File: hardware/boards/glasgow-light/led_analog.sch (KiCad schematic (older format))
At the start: 10 parts, among them U1 LM358_DFN

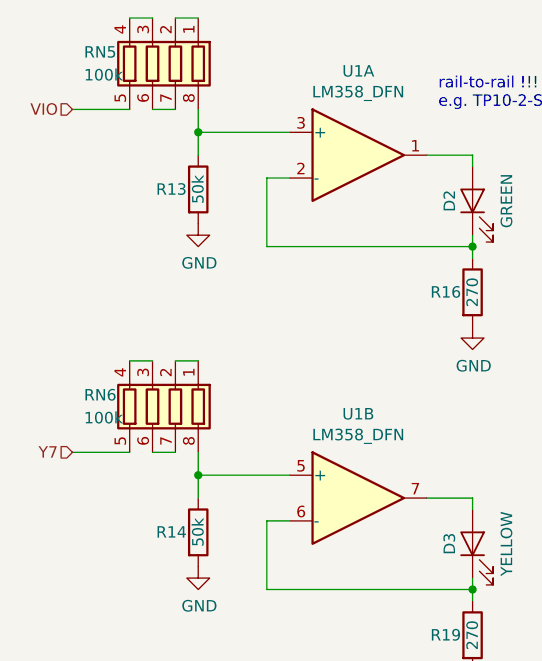
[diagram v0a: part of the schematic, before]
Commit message: add alternative resistors
We might not want to place any resistor arrays on the bottom side
because we will most likely hand-solder it.
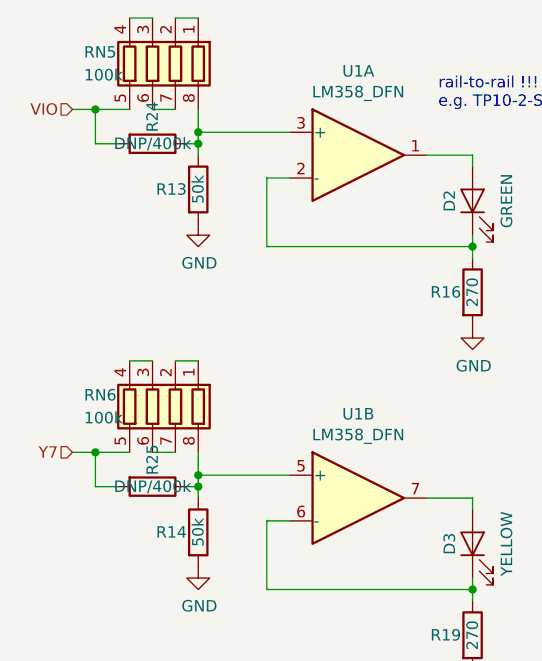
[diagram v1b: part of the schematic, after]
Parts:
- added R24, R25: DNP/400k, Resistor_SMD:R_0402_1005Metric, symbol Device:R
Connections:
- net VIO: now also R24.2
- net Y7: now also R25.2
- net at R13.1, RN5.8 (R1.2), U1.3 (+): now also R24.1
- net at R14.1, RN6.8 (R1.2), U1.5 (+): now also R25.1
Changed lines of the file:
@@
 	5000 3400 5000 3300
 Wire Wire Line
-	5000 3400 5000 3500
+	5000 3400 5000 3450
 Connection ~ 5000 3400
 $Comp
@@
 	4800 2900 4700 2900
 Wire Wire Line
-	4700 3300 4450 3300
+	4700 3300 4550 3300
 $Comp
 L Amplifier_Operational:LM358_DFN U1
@@
 	5000 4900 5000 4800
 Wire Wire Line
-	5000 4900 5000 5000
+	5000 4900 5000 4950
 Connection ~ 5000 4900
 $Comp
@@
 	4800 4400 4700 4400
 Wire Wire Line
-	4700 4800 4450 4800
+	4700 4800 4550 4800
 $Comp
 L Device:R R?
@@
 Wire Wire Line
 	7900 4250 8000 4250
+$Comp
+L Device:R R?
+U 1 1 6000E9AC
+P 4800 4950
+AR Path="/5AF7D604/6000E9AC" Ref="R?"  Part="1"
+AR Path="/5AFBDC9E/6000E9AC" Ref="R?"  Part="1"
+AR Path="/5C7B59B0/5C9E337E/6000E9AC" Ref="R?"  Part="1"
+AR Path="/5C7B59B0/5C9E338E/6000E9AC" Ref="R?"  Part="1"
+AR Path="/5FFD4B90/6000E9AC" Ref="R?"  Part="1"
+AR Path="/5FFD4BA1/6000E9AC" Ref="R?"  Part="1"
+AR Path="/5C7B59B0/5C9E337E/60515668/6000E9AC" Ref="R25"  Part="1"
+F 0 "R25" H 4750 4950 50  0000 R CNN
+F 1 "DNP/400k" V 4800 4950 50  0000 C CNN
+F 2 "Resistor_SMD:R_0402_1005Metric" V 4730 4950 50  0001 C CNN
+F 3 "https://www.mouser.com/datasheet/2/447/PYu-RC_Group_51_RoHS_L_10-1527934.pdf" H 4800 4950 50  0001 C CNN
+F 4 "Yageo" H -1350 0   50  0001 C CNN "Mfg"
+F 5 "RC0402FR-132K2L" H -1350 0   50  0001 C CNN "MPN"
+F 6 "res-0402-2k2" H 4800 4950 50  0001 C CNN "1b2-bom-key"
+	1    4800 4950
+	0    1    1    0
+$EndComp
+Wire Wire Line
+	4950 4950 5000 4950
+Connection ~ 5000 4950
+Wire Wire Line
+	5000 4950 5000 5000
+Wire Wire Line
+	4650 4950 4550 4950
+Wire Wire Line
+	4550 4950 4550 4800
+Connection ~ 4550 4800
+Wire Wire Line
+	4550 4800 4450 4800
+$Comp
+L Device:R R?
+U 1 1 600129BB
+P 4800 3450
+AR Path="/5AF7D604/600129BB" Ref="R?"  Part="1"
+AR Path="/5AFBDC9E/600129BB" Ref="R?"  Part="1"
+AR Path="/5C7B59B0/5C9E337E/600129BB" Ref="R?"  Part="1"
+AR Path="/5C7B59B0/5C9E338E/600129BB" Ref="R?"  Part="1"
+AR Path="/5FFD4B90/600129BB" Ref="R?"  Part="1"
+AR Path="/5FFD4BA1/600129BB" Ref="R?"  Part="1"
+AR Path="/5C7B59B0/5C9E337E/60515668/600129BB" Ref="R24"  Part="1"
+F 0 "R24" H 4750 3450 50  0000 R CNN
+F 1 "DNP/400k" V 4800 3450 50  0000 C CNN
+F 2 "Resistor_SMD:R_0402_1005Metric" V 4730 3450 50  0001 C CNN
+F 3 "https://www.mouser.com/datasheet/2/447/PYu-RC_Group_51_RoHS_L_10-1527934.pdf" H 4800 3450 50  0001 C CNN
+F 4 "Yageo" H -1350 -1500 50  0001 C CNN "Mfg"
+F 5 "RC0402FR-132K2L" H -1350 -1500 50  0001 C CNN "MPN"
+F 6 "res-0402-2k2" H 4800 3450 50  0001 C CNN "1b2-bom-key"
+	1    4800 3450
+	0    1    1    0
+$EndComp
+Wire Wire Line
+	4950 3450 5000 3450
+Connection ~ 5000 3450
+Wire Wire Line
+	5000 3450 5000 3500
+Wire Wire Line
+	4650 3450 4550 3450
+Wire Wire Line
+	4550 3450 4550 3300
+Connection ~ 4550 3300
+Wire Wire Line
+	4550 3300 4450 3300
 $EndSCHEMATC
